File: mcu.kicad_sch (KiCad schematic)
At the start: 34 parts, among them J201 Connector, USB-TYPE-C-16P, SW201 SK-12D02, U1 STM32F723VET6, U2 USBLC6-2SC6, U201 TS3USB221ARSER, X1 16MHz

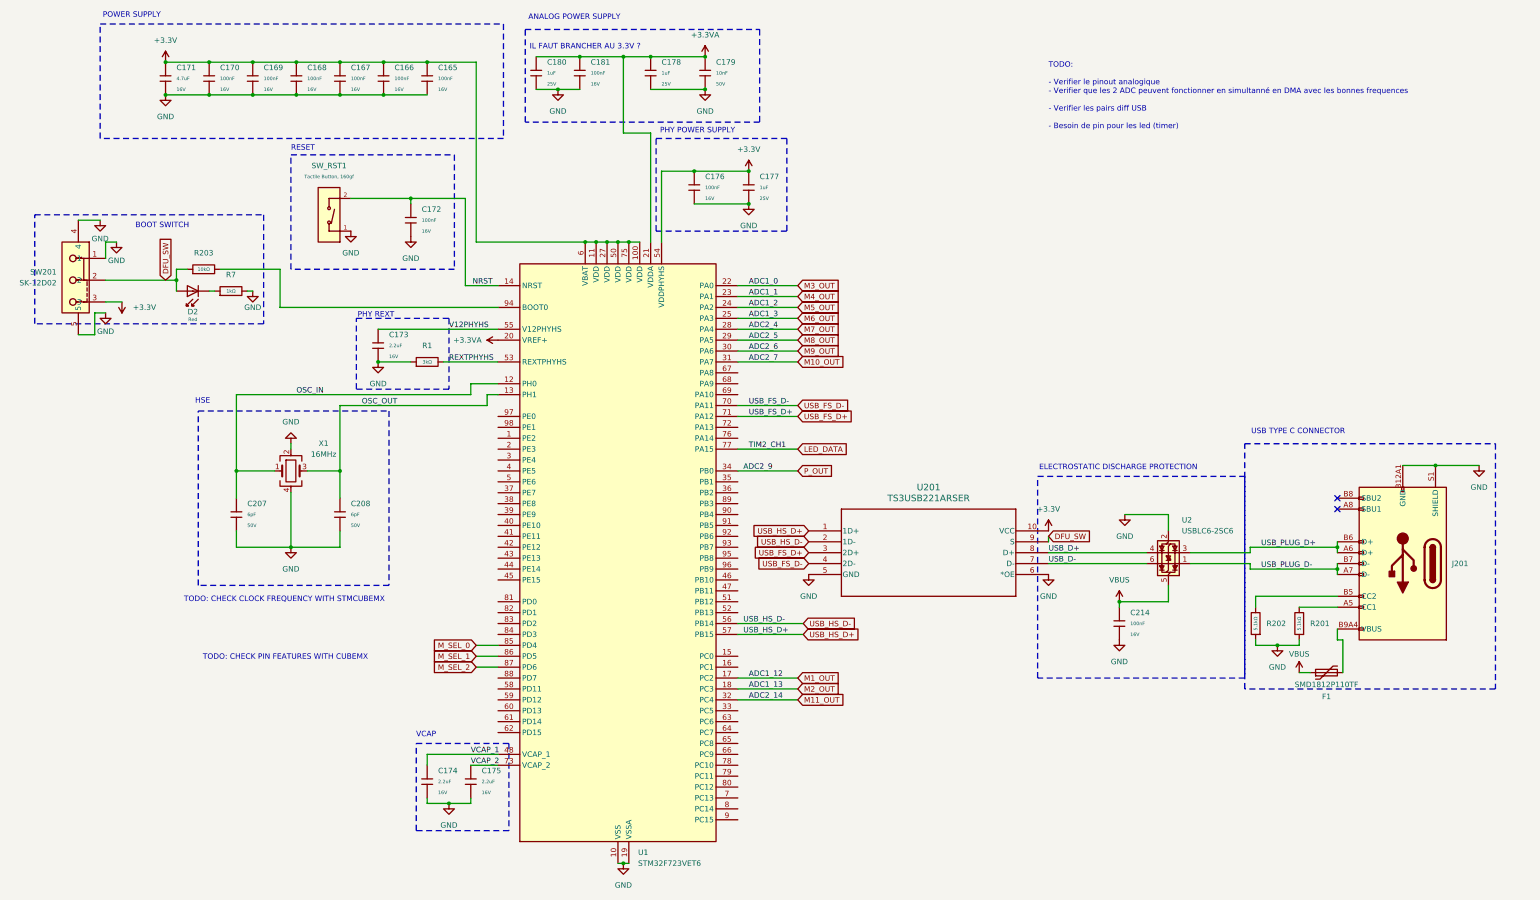
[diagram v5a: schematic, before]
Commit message: add fuse & continue usb
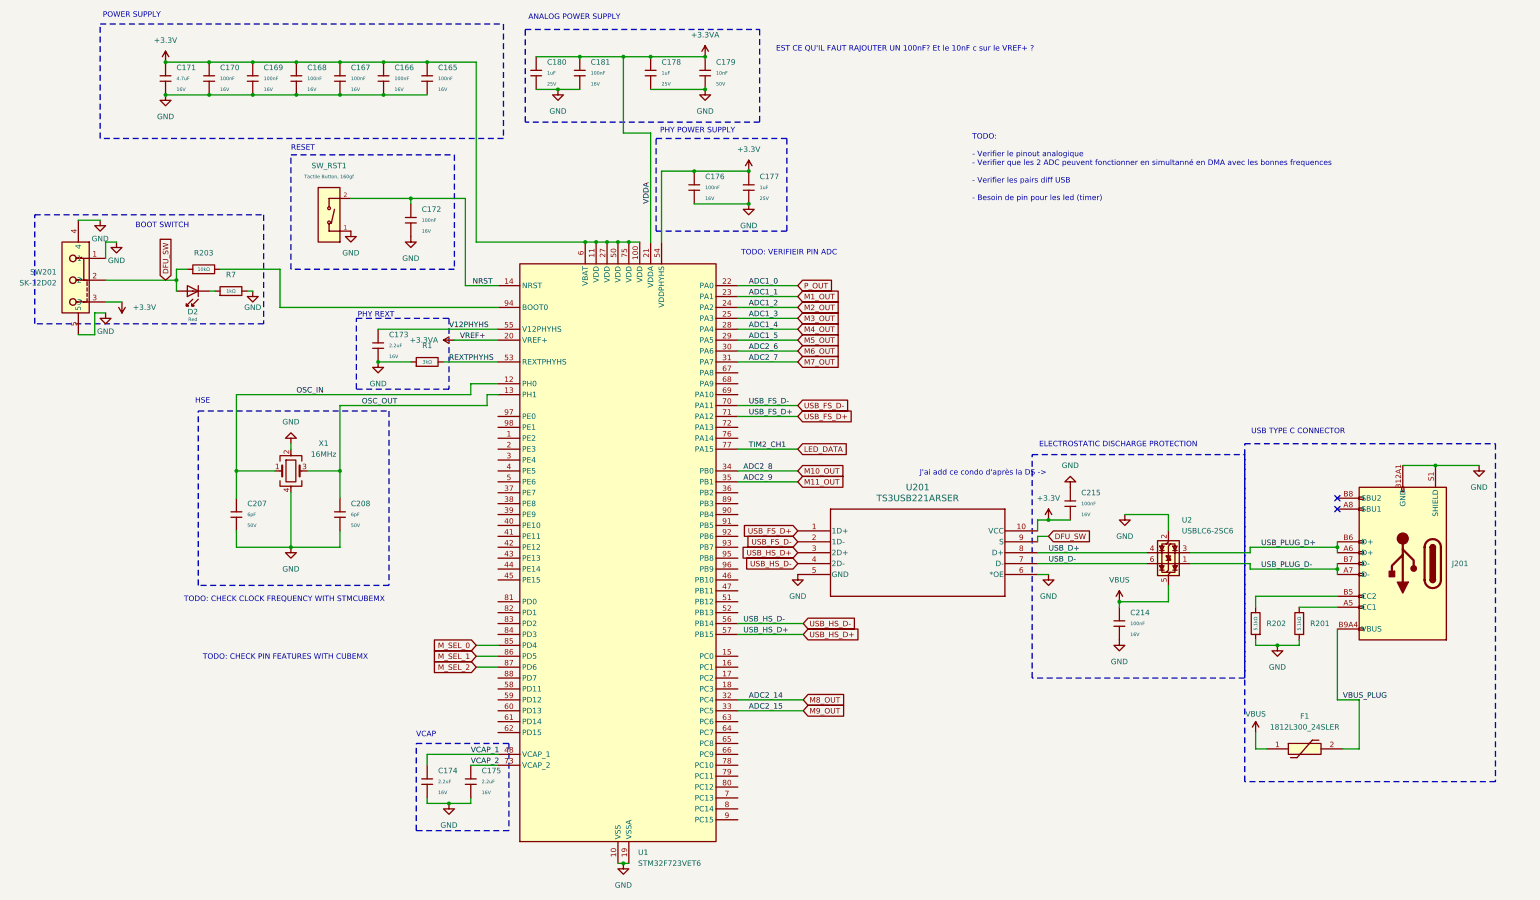
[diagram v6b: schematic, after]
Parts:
- removed F1: SMD1812P110TF, Fuse:Fuse_1812_4532Metric, symbol Device:Polyfuse
- removed U201: TS3USB221ARSER, footprints:RSE10, symbol 2025-12-06_14-23-22:TS3USB221ARSER
- added C215: 100nF, PCM_JLCPCB:C_0402, symbol PCM_JLCPCB-Capacitors:0402,100nF
- added F1: 1812L300_24SLER, 1812L190SLPR, symbol 1812L300_24SLER:1812L300_24SLER
- added U201: TS3USB221ARSER, TS3USB221ARSER:RSE10, symbol TS3USB221ARSER:TS3USB221ARSER
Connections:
- net +3.3V: now also C215.2, U201.10 (VCC)
- net DFU_SW: now also U201.9 (S)
- net GND: now also C215.1, U201.5 (GND), U201.6 (*OE)
- net M10_OUT: now also U1.34 (PB0); no longer U1.31 (PA7)
- net M11_OUT: now also U1.35 (PB1); no longer U1.32 (PC4)
- net M1_OUT: now also U1.23 (PA1); no longer U1.17 (PC2)
- net M2_OUT: now also U1.24 (PA2); no longer U1.18 (PC3)
- net M3_OUT: now also U1.25 (PA3); no longer U1.22 (PA0)
- net M4_OUT: now also U1.28 (PA4); no longer U1.23 (PA1)
- net M5_OUT: now also U1.29 (PA5); no longer U1.24 (PA2)
- net M6_OUT: now also U1.30 (PA6); no longer U1.25 (PA3)
- net M7_OUT: now also U1.31 (PA7); no longer U1.28 (PA4)
- net M8_OUT: now also U1.32 (PC4); no longer U1.29 (PA5)
- net M9_OUT: now also U1.33 (PC5); no longer U1.30 (PA6)
- net P_OUT: now also U1.22 (PA0); no longer U1.34 (PB0)
- net USB_D+: now also U201.8 (D+)
- net USB_D-: now also U201.7 (D-)
- net USB_FS_D+: now also U201.1 (1D+)
- net USB_FS_D-: now also U201.2 (1D-)
- net USB_HS_D+: now also U201.3 (2D+)
- net USB_HS_D-: now also U201.4 (2D-)
- net VBUS: now also F1.1
- net VBUS_PLUG: now reaches J201.A9B4 (VBUS), J201.B9A4 (VBUS)
- net VBUS_PLUG: now also F1.2
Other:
- note added: "EST CE QU'IL FAUT RAJOUTER UN 100nF? Et le 10nF c sur le VREF+ ?"
- note added: "J'ai add ce condo d'après la DS ->"
- note added: "TODO: VERIFIEIR PIN ADC"
- note removed: "IL FAUT BRANCHER AU 3.3V ?"

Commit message: vdda power supply & sensor decoupling capacitor
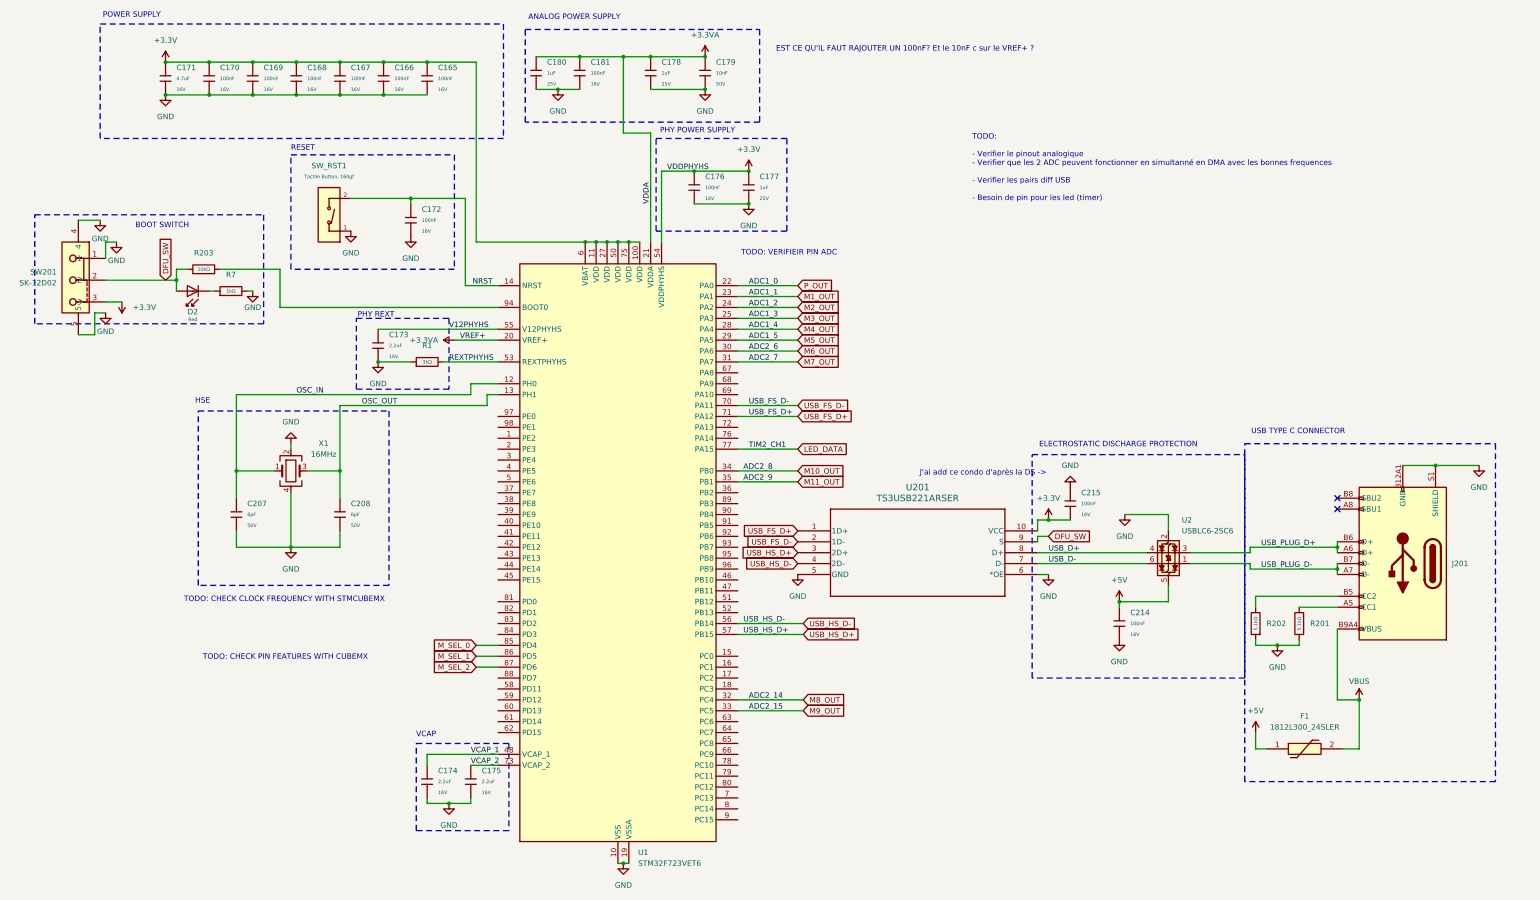
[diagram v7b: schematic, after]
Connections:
- net VBUS_PLUG is gone; now on net VBUS: F1.2, J201.A9B4 (VBUS), J201.B9A4 (VBUS)
- net VBUS: no longer C214.1, F1.1, U2.5 (VBUS)
- new net +5V: C214.1, F1.1, U2.5 (VBUS)
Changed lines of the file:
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@@
 	)
 	(junction
+		(at 373.38 173.99)
+		(diameter 0)
+		(color 0 0 0 0)
+	)
+	(junction
 		(at 105.41 25.4)
 		(diameter 0)
@@
 		)
 	)
+	(label "VDDPHYHS"
+		(at 212.09 50.8 0)
+		(effects
+			(font
+				(size 1.27 1.27)
+			)
+			(justify left bottom)
+		)
+	)
 	(label "VREF+"
 		(at 163.83 90.17 0)
@@
 		)
 	)
-	(label "VBUS_PLUG"
-		(at 369.57 173.99 0)
-		(effects
-			(font
-				(size 1.27 1.27)
-			)
-			(justify left bottom)
-		)
-	)
 	(label "USB_FS_D-"
 		(at 231.14 105.41 0)
@@
 	)
 	(symbol
+		(lib_id "power:+5V")
+		(at 317.5 151.13 0)
+		(unit 1)
+		(exclude_from_sim no)
+		(in_bom yes)
+		(on_board yes)
+		(dnp no)
+		(fields_autoplaced yes)
+		(property "Reference" "#PWR0236"
+			(at 317.5 154.94 0)
+			(effects
+				(font
+					(size 1.27 1.27)
+				)
+				(hide yes)
+			)
+		)
+		(property "Value" "+5V"
+			(at 317.5 146.05 0)
+			(effects
+				(font
+					(size 1.27 1.27)
+				)
+			)
+		)
+		(property "Footprint" ""
+			(at 317.5 151.13 0)
+			(effects
+				(font
+					(size 1.27 1.27)
+				)
+				(hide yes)
+			)
+		)
+		(property "Datasheet" ""
+			(at 317.5 151.13 0)
+			(effects
+				(font
+					(size 1.27 1.27)
+				)
+				(hide yes)
+			)
+		)
+		(property "Description" "Power symbol creates a global label with name \"+5V\""
+			(at 317.5 151.13 0)
+			(effects
+				(font
+					(size 1.27 1.27)
+				)
+				(hide yes)
+			)
+		)
+		(pin "1"
+		)
+		(instances
+			(project "75he"
+				(path "/0edb4e17-93a4-4f7b-ad91-3a5c72b69d23/e7ec310e-33d9-421e-aaaf-42ca5ffe1b35"
+					(reference "#PWR0236")
+					(unit 1)
+				)
+			)
+		)
+	)
+	(symbol
 		(lib_id "1812L300_24SLER:1812L300_24SLER")
 		(at 351.79 185.42 0)
@@
 	)
 	(symbol
-		(lib_id "power:VBUS")
-		(at 317.5 151.13 0)
+		(lib_id "power:+5V")
+		(at 349.25 181.61 0)
 		(unit 1)
 		(exclude_from_sim no)
@@
 		(dnp no)
 		(fields_autoplaced yes)
-		(property "Reference" "#PWR0221"
-			(at 317.5 154.94 0)
+		(property "Reference" "#PWR0235"
+			(at 349.25 185.42 0)
 			(effects
 				(font
@@
 			)
 		)
-		(property "Value" "VBUS"
-			(at 317.5 146.05 0)
+		(property "Value" "+5V"
+			(at 349.25 176.53 0)
 			(effects
 				(font
@@
 		)
 		(property "Footprint" ""
-			(at 317.5 151.13 0)
+			(at 349.25 181.61 0)
 			(effects
 				(font
@@
 		)
 		(property "Datasheet" ""
-			(at 317.5 151.13 0)
+			(at 349.25 181.61 0)
 			(effects
 				(font
@@
 			)
 		)
-		(property "Description" "Power symbol creates a global label with name \"VBUS\""
-			(at 317.5 151.13 0)
+		(property "Description" "Power symbol creates a global label with name \"+5V\""
+			(at 349.25 181.61 0)
 			(effects
 				(font
@@
 		)
 		(instances
-			(project "75he"
+			(project ""
 				(path "/0edb4e17-93a4-4f7b-ad91-3a5c72b69d23/e7ec310e-33d9-421e-aaaf-42ca5ffe1b35"
-					(reference "#PWR0221")
+					(reference "#PWR0235")
 					(unit 1)
 				)
@@
 	(symbol
 		(lib_id "power:VBUS")
-		(at 349.25 181.61 0)
+		(at 373.38 173.99 0)
 		(unit 1)
 		(exclude_from_sim no)
@@
 		(dnp no)
 		(property "Reference" "#PWR0219"
-			(at 349.25 185.42 0)
+			(at 373.38 177.8 0)
 			(effects
 				(font
@@
 		)
 		(property "Value" "VBUS"
-			(at 349.25 177.292 0)
+			(at 373.38 169.672 0)
 			(effects
 				(font
@@
 		)
 		(property "Footprint" ""
-			(at 349.25 181.61 0)
+			(at 373.38 173.99 0)
 			(effects
 				(font
@@
 		)
 		(property "Datasheet" ""
-			(at 349.25 181.61 0)
+			(at 373.38 173.99 0)
 			(effects
 				(font
@@
 		)
 		(property "Description" "Power symbol creates a global label with name \"VBUS\""
-			(at 349.25 181.61 0)
+			(at 373.38 173.99 0)
 			(effects
 				(font
@@
 		)
 		(instances
-			(project ""
+			(project "75he"
 				(path "/0edb4e17-93a4-4f7b-ad91-3a5c72b69d23/e7ec310e-33d9-421e-aaaf-42ca5ffe1b35"
 					(reference "#PWR0219")

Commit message: caca
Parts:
- added C216: 100nF, PCM_JLCPCB:C_0402, symbol PCM_JLCPCB-Capacitors:0402,100nF
- added C217: 1uF, PCM_JLCPCB:C_0402, symbol PCM_JLCPCB-Capacitors:0402,1uF
- added IC1: SN74AHCT1G125DBVR, SamacSys_Parts:SOT95P280X145-5N, symbol SamacSys_Parts:SN74AHCT1G125DBVR
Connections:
- net +5V: now also C216.1, C217.1, IC1.5 (VCC)
- net GND: now also C216.2, C217.2, IC1.1 (~{OE}), IC1.3 (GND)
- net LED_DATA: now also IC1.2 (A)
- new net LED_DATA_5V: IC1.4 (Y)
- no-connect marks 2 -> 59
